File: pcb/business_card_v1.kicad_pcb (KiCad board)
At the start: 16 copper layers, 89 x 51 mm, 70 parts, among them J1 Conn_01x05_Male, J2 Conn_01x01_Male, SW1 SW_SPST, U1 MIC5504-3.3YM5, U2 STM32G030F6P6

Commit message: cleanup
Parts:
- removed J2: Conn_01x01_Male, Connector_PinSocket_2.54mm:PinSocket_1x01_P2.54mm_Vertical
- removed REF**: OSHW-Symbol_6.7x6mm_SilkScreen, Symbol:OSHW-Symbol_6.7x6mm_SilkScreen
- removed REF**: KiCad-Logo_6mm_SilkScreen, Symbol:KiCad-Logo_6mm_SilkScreen
- J1: moved to F.Cu
- RN1, RN2: footprint Resistor_SMD:R_Array_Convex_4x0603 -> Resistor_SMD:R_Array_Convex_4x1206
- SW1: value SW_SPST -> SPST_TACT-KMR2
- moved J1 10.2 mm to (132.1, 126.7)
- moved C2 1.27 mm to (126.4, 116.8)
- moved C3 1.27 mm to (128.3, 116.8)
- moved U1 1.27 mm to (127.0, 121.3)
- moved RN1 0.13 mm to (146.7, 118.1)
- moved RN2 0.13 mm to (146.7, 125.7)
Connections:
- J1 pad 2: SWDCLK-BOOT0 -> SWDIO
- J1 pad 4: SWDIO -> SWDCLK-BOOT0
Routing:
- net PINC: track 11.5 -> 13.8 mm, vias 2 -> 0
- net PINH: track 10.2 -> 8.94 mm
- net GND: track 14.6 -> 13.3 mm
- net PING: track 13.8 -> 12.8 mm, vias 2 -> 0
- net Net-(LED1-PadA): track 104.9 -> 103.8 mm
- net PINA: track 15.3 -> 16.4 mm
- net PINE: track 17.7 -> 18.7 mm
- net +5V: track 19.9 -> 20.8 mm
- net Net-(LED14-PadA): track 136.4 -> 135.6 mm
- net Net-(LED10-PadA): track 106.4 -> 105.6 mm
- net +3V3: track 1.79 -> 1.13 mm
- net Net-(LED11-PadA): track 123.5 -> 122.8 mm
- net Net-(LED10-PadC): track 136.8 -> 136.1 mm
- net Net-(LED13-PadA): track 136.1 -> 135.6 mm
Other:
- board text added: "B.E. Electrical Engineering & B.Sc. Computer Science"
- board text added: "Website: kevin.lutzer.ca Email: kevin@lutzer.ca Github: github.com/kevinlutzer LinkedIn: linkedin.com/in/kevin-lutzer"
- board text added: "v2.1"
- board text removed: "3.3V-REF"
- board text removed: "5v-SUP"
- board text removed: "B.E. Electrical Engineering & B.Sc. Computer Science Website: kevin.lutzer.ca Email: kevin@lutzer.ca Github: github.com/kevinlutzer LinkedIn: linkedin.com/in/kevin-lutzer"
- board text removed: "GND"
- board text removed: "RST"
- board text removed: "SWDCLK"
- board text removed: "SWDIO"
- board text removed: "designed with"
- board text removed: "open source"
- board text removed: "v3"

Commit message: remove the v3
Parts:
- added J2: Conn_01x01_Male, Connector_PinSocket_2.54mm:PinSocket_1x01_P2.54mm_Vertical, B.Cu at (122.5, 116.5)
- added REF**: OSHW-Symbol_6.7x6mm_SilkScreen, Symbol:OSHW-Symbol_6.7x6mm_SilkScreen, B.Cu at (141.2, 86.6)
- added REF**: KiCad-Logo_6mm_SilkScreen, Symbol:KiCad-Logo_6mm_SilkScreen, B.Cu at (114.8, 86.6)
- J1: moved to B.Cu
- RN1, RN2: footprint Resistor_SMD:R_Array_Convex_4x1206 -> Resistor_SMD:R_Array_Convex_4x0603
- SW1: value SPST_TACT-KMR2 -> SW_SPST
- moved J1 10.2 mm to (132.1, 116.5)
- moved C2 1.27 mm to (126.4, 115.6)
- moved C3 1.27 mm to (128.3, 115.6)
- moved U1 1.27 mm to (127.0, 120.0)
- moved RN1 0.13 mm to (146.6, 118.1)
- moved RN2 0.13 mm to (146.6, 125.7)
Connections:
- J1 pad 2: SWDIO -> SWDCLK-BOOT0
- J1 pad 4: SWDCLK-BOOT0 -> SWDIO
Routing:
- net PINC: track 13.8 -> 11.5 mm, vias 0 -> 2
- net PINH: track 8.94 -> 10.2 mm
- net GND: track 13.3 -> 14.6 mm
- net PING: track 12.8 -> 13.8 mm, vias 0 -> 2
- net Net-(LED1-PadA): track 103.8 -> 104.9 mm
- net PINA: track 16.4 -> 15.3 mm
- net PINE: track 18.7 -> 17.7 mm
- net +5V: track 20.8 -> 19.9 mm
- net Net-(LED14-PadA): track 135.6 -> 136.4 mm
- net Net-(LED10-PadA): track 105.6 -> 106.4 mm
- net +3V3: track 1.13 -> 1.79 mm
- net Net-(LED11-PadA): track 122.8 -> 123.5 mm
- net Net-(LED10-PadC): track 136.1 -> 136.8 mm
- net Net-(LED13-PadA): track 135.6 -> 136.1 mm
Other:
- board text added: "3.3V-REF"
- board text added: "5v-SUP"
- board text added: "B.E. Electrical Engineering & B.Sc. Computer Science Website: kevin.lutzer.ca Email: kevin@lutzer.ca Github: github.com/kevinlutzer LinkedIn: linkedin.com/in/kevin-lutzer"
- board text added: "GND"
- board text added: "RST"
- board text added: "SWDCLK"
- board text added: "SWDIO"
- board text added: "designed with"
- board text added: "open source"
- board text added: "v3"
- board text removed: "B.E. Electrical Engineering & B.Sc. Computer Science"
- board text removed: "Website: kevin.lutzer.ca Email: kevin@lutzer.ca Github: github.com/kevinlutzer LinkedIn: linkedin.com/in/kevin-lutzer"
- board text removed: "v2.1"

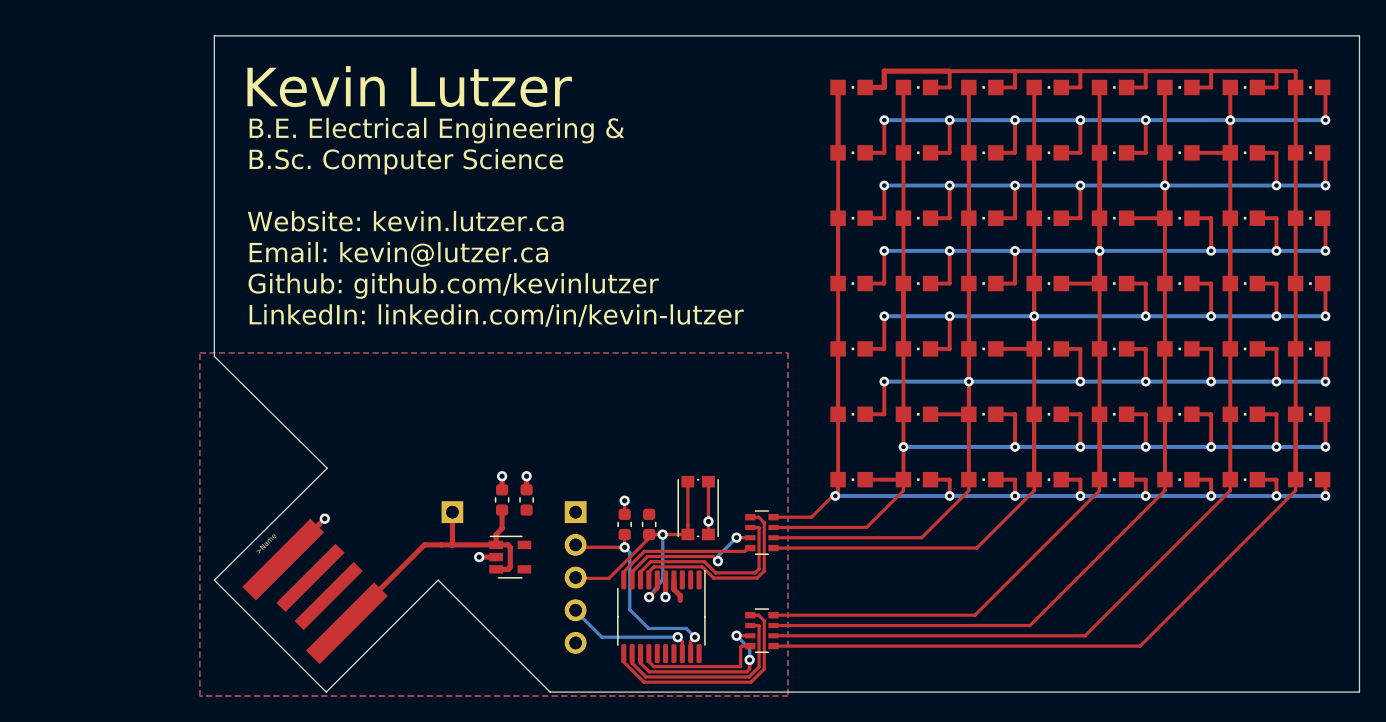
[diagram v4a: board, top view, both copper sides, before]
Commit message: realign components on 0.01 inch grid, use solely kicad parts not eagle parts
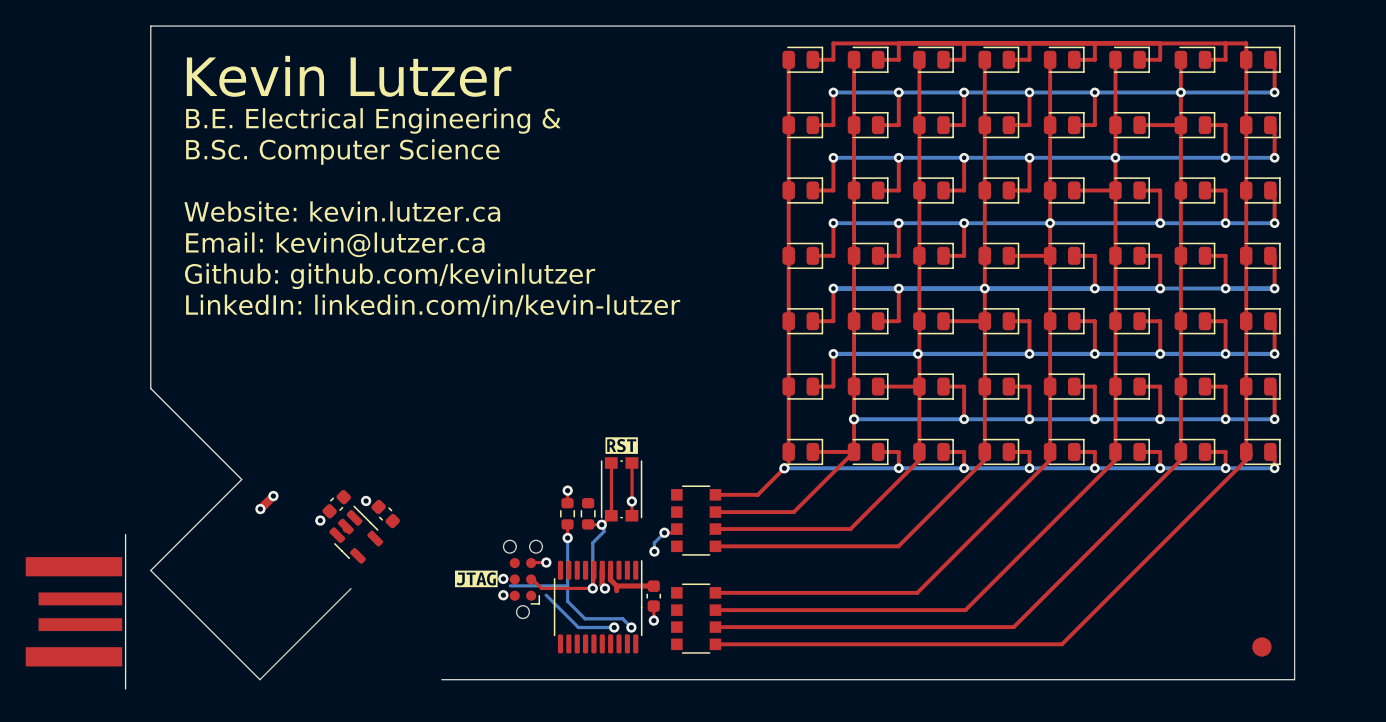
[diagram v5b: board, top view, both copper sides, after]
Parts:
- removed C3: 1u, Capacitor_SMD:C_0603_1608Metric
- removed J1: Conn_01x05_Male, Connector_PinHeader_2.54mm:PinHeader_1x05_P2.54mm_Vertical
- removed J2: Conn_01x01_Male, Connector_PinSocket_2.54mm:PinSocket_1x01_P2.54mm_Vertical
- removed JP1: USBPCB, business_card_v1:USB-A-PCB
- removed LED3: LEDCHIPLED_0805, business_card_v1:CHIPLED_0805
- removed R10: 10K, Resistor_SMD:R_0603_1608Metric
- removed the REF** at (141.2, 86.6)
- removed the REF** at (114.8, 86.6)
- added C1: 100n, Capacitor_SMD:C_0603_1608Metric, F.Cu at (138.2, 123.0)
- added C4: 1u, Capacitor_SMD:C_0603_1608Metric, F.Cu at (113.5, 115.9)
- added D7: LED, Diode_SMD:D_0805_2012Metric, F.Cu at (159.7, 81.4)
- added J3: USB_A, Kevin_Lutzer_Lbr:USB_A_PCB, F.Cu at (93.3, 124.3)
- added J4: Conn_ARM_SWD_TagConnect_TC2030, Connector:Tag-Connect_TC2030-IDC-NL_2x03_P1.27mm_Vertical, F.Cu at (128.0, 121.7)
- added R2: 10k, Resistor_SMD:R_0603_1608Metric, F.Cu at (131.5, 116.6)
- added REF**: Fiducial_1.5mm_Mask3mm, Fiducial:Fiducial_1.5mm_Mask3mm, F.Cu at (185.4, 127.0)
- added kibuzzard-64BD9765: G***, kibuzzard-64BD9765, F.Cu at (135.7, 111.3)
- added kibuzzard-64BD977B: G***, kibuzzard-64BD977B, F.Cu at (124.4, 121.7)
- D1: renamed from LED9; value LEDCHIPLED_0805 -> LED; footprint business_card_v1:CHIPLED_0805 -> Diode_SMD:D_0805_2012Metric
- D10: renamed from LED27; value LEDCHIPLED_0805 -> LED; footprint business_card_v1:CHIPLED_0805 -> Diode_SMD:D_0805_2012Metric
- D11: renamed from LED4; value LEDCHIPLED_0805 -> LED; footprint business_card_v1:CHIPLED_0805 -> Diode_SMD:D_0805_2012Metric
- D12: renamed from LED12; value LEDCHIPLED_0805 -> LED; footprint business_card_v1:CHIPLED_0805 -> Diode_SMD:D_0805_2012Metric
- D13: renamed from LED20; value LEDCHIPLED_0805 -> LED; footprint business_card_v1:CHIPLED_0805 -> Diode_SMD:D_0805_2012Metric
- D14: renamed from LED28; value LEDCHIPLED_0805 -> LED; footprint business_card_v1:CHIPLED_0805 -> Diode_SMD:D_0805_2012Metric
- D15: renamed from LED5; value LEDCHIPLED_0805 -> LED; footprint business_card_v1:CHIPLED_0805 -> Diode_SMD:D_0805_2012Metric
- D16: renamed from LED13; value LEDCHIPLED_0805 -> LED; footprint business_card_v1:CHIPLED_0805 -> Diode_SMD:D_0805_2012Metric
- D17: renamed from LED21; value LEDCHIPLED_0805 -> LED; footprint business_card_v1:CHIPLED_0805 -> Diode_SMD:D_0805_2012Metric
- D18: renamed from LED29; value LEDCHIPLED_0805 -> LED; footprint business_card_v1:CHIPLED_0805 -> Diode_SMD:D_0805_2012Metric
- D19: renamed from LED6; value LEDCHIPLED_0805 -> LED; footprint business_card_v1:CHIPLED_0805 -> Diode_SMD:D_0805_2012Metric
- D2: renamed from LED17; value LEDCHIPLED_0805 -> LED; footprint business_card_v1:CHIPLED_0805 -> Diode_SMD:D_0805_2012Metric
- D20: renamed from LED14; value LEDCHIPLED_0805 -> LED; footprint business_card_v1:CHIPLED_0805 -> Diode_SMD:D_0805_2012Metric
- D21: renamed from LED22; value LEDCHIPLED_0805 -> LED; footprint business_card_v1:CHIPLED_0805 -> Diode_SMD:D_0805_2012Metric
- D22: renamed from LED30; value LEDCHIPLED_0805 -> LED; footprint business_card_v1:CHIPLED_0805 -> Diode_SMD:D_0805_2012Metric
- D23: renamed from LED7; value LEDCHIPLED_0805 -> LED; footprint business_card_v1:CHIPLED_0805 -> Diode_SMD:D_0805_2012Metric
- D24: renamed from LED15; value LEDCHIPLED_0805 -> LED; footprint business_card_v1:CHIPLED_0805 -> Diode_SMD:D_0805_2012Metric
- D25: renamed from LED23; value LEDCHIPLED_0805 -> LED; footprint business_card_v1:CHIPLED_0805 -> Diode_SMD:D_0805_2012Metric
- D26: renamed from LED8; value LEDCHIPLED_0805 -> LED; footprint business_card_v1:CHIPLED_0805 -> Diode_SMD:D_0805_2012Metric
- D27: renamed from LED16; value LEDCHIPLED_0805 -> LED; footprint business_card_v1:CHIPLED_0805 -> Diode_SMD:D_0805_2012Metric
- D28: renamed from LED24; value LEDCHIPLED_0805 -> LED; footprint business_card_v1:CHIPLED_0805 -> Diode_SMD:D_0805_2012Metric
- D29: renamed from LED33; value LEDCHIPLED_0805 -> LED; footprint business_card_v1:CHIPLED_0805 -> Diode_SMD:D_0805_2012Metric
- D3: renamed from LED25; value LEDCHIPLED_0805 -> LED; footprint business_card_v1:CHIPLED_0805 -> Diode_SMD:D_0805_2012Metric
- D30: renamed from LED41; value LEDCHIPLED_0805 -> LED; footprint business_card_v1:CHIPLED_0805 -> Diode_SMD:D_0805_2012Metric
- D31: renamed from LED49; value LEDCHIPLED_0805 -> LED; footprint business_card_v1:CHIPLED_0805 -> Diode_SMD:D_0805_2012Metric
- D32: renamed from LED34; value LEDCHIPLED_0805 -> LED; footprint business_card_v1:CHIPLED_0805 -> Diode_SMD:D_0805_2012Metric
- D33: renamed from LED42; value LEDCHIPLED_0805 -> LED; footprint business_card_v1:CHIPLED_0805 -> Diode_SMD:D_0805_2012Metric
- D34: renamed from LED50; value LEDCHIPLED_0805 -> LED; footprint business_card_v1:CHIPLED_0805 -> Diode_SMD:D_0805_2012Metric
- D35: renamed from LED35; value LEDCHIPLED_0805 -> LED; footprint business_card_v1:CHIPLED_0805 -> Diode_SMD:D_0805_2012Metric
- D36: renamed from LED43; value LEDCHIPLED_0805 -> LED; footprint business_card_v1:CHIPLED_0805 -> Diode_SMD:D_0805_2012Metric
- D37: renamed from LED51; value LEDCHIPLED_0805 -> LED; footprint business_card_v1:CHIPLED_0805 -> Diode_SMD:D_0805_2012Metric
- D38: renamed from LED36; value LEDCHIPLED_0805 -> LED; footprint business_card_v1:CHIPLED_0805 -> Diode_SMD:D_0805_2012Metric
- D39: renamed from LED44; value LEDCHIPLED_0805 -> LED; footprint business_card_v1:CHIPLED_0805 -> Diode_SMD:D_0805_2012Metric
- D4: renamed from LED10; value LEDCHIPLED_0805 -> LED; footprint business_card_v1:CHIPLED_0805 -> Diode_SMD:D_0805_2012Metric
- D40: renamed from LED52; value LEDCHIPLED_0805 -> LED; footprint business_card_v1:CHIPLED_0805 -> Diode_SMD:D_0805_2012Metric
- D41: renamed from LED37; value LEDCHIPLED_0805 -> LED; footprint business_card_v1:CHIPLED_0805 -> Diode_SMD:D_0805_2012Metric
- D42: renamed from LED45; value LEDCHIPLED_0805 -> LED; footprint business_card_v1:CHIPLED_0805 -> Diode_SMD:D_0805_2012Metric
- D43: renamed from LED53; value LEDCHIPLED_0805 -> LED; footprint business_card_v1:CHIPLED_0805 -> Diode_SMD:D_0805_2012Metric
- D44: renamed from LED38; value LEDCHIPLED_0805 -> LED; footprint business_card_v1:CHIPLED_0805 -> Diode_SMD:D_0805_2012Metric
- D45: renamed from LED46; value LEDCHIPLED_0805 -> LED; footprint business_card_v1:CHIPLED_0805 -> Diode_SMD:D_0805_2012Metric
- D46: renamed from LED54; value LEDCHIPLED_0805 -> LED; footprint business_card_v1:CHIPLED_0805 -> Diode_SMD:D_0805_2012Metric
- D47: renamed from LED31; value LEDCHIPLED_0805 -> LED; footprint business_card_v1:CHIPLED_0805 -> Diode_SMD:D_0805_2012Metric
- D48: renamed from LED39; value LEDCHIPLED_0805 -> LED; footprint business_card_v1:CHIPLED_0805 -> Diode_SMD:D_0805_2012Metric
- D49: renamed from LED47; value LEDCHIPLED_0805 -> LED; footprint business_card_v1:CHIPLED_0805 -> Diode_SMD:D_0805_2012Metric
- D5: renamed from LED18; value LEDCHIPLED_0805 -> LED; footprint business_card_v1:CHIPLED_0805 -> Diode_SMD:D_0805_2012Metric
- D50: renamed from LED55; value LEDCHIPLED_0805 -> LED; footprint business_card_v1:CHIPLED_0805 -> Diode_SMD:D_0805_2012Metric
- D51: renamed from LED32; value LEDCHIPLED_0805 -> LED; footprint business_card_v1:CHIPLED_0805 -> Diode_SMD:D_0805_2012Metric
- D52: renamed from LED40; value LEDCHIPLED_0805 -> LED; footprint business_card_v1:CHIPLED_0805 -> Diode_SMD:D_0805_2012Metric
- D53: renamed from LED48; value LEDCHIPLED_0805 -> LED; footprint business_card_v1:CHIPLED_0805 -> Diode_SMD:D_0805_2012Metric
- D54: renamed from LED56; value LEDCHIPLED_0805 -> LED; footprint business_card_v1:CHIPLED_0805 -> Diode_SMD:D_0805_2012Metric
- D6: renamed from LED26; value LEDCHIPLED_0805 -> LED; footprint business_card_v1:CHIPLED_0805 -> Diode_SMD:D_0805_2012Metric
- D8: renamed from LED11; value LEDCHIPLED_0805 -> LED; footprint business_card_v1:CHIPLED_0805 -> Diode_SMD:D_0805_2012Metric
- D9: renamed from LED19; value LEDCHIPLED_0805 -> LED; footprint business_card_v1:CHIPLED_0805 -> Diode_SMD:D_0805_2012Metric
- LED1, LED2: footprint business_card_v1:CHIPLED_0805 -> Diode_SMD:D_0805_2012Metric
- R1: value 10K -> 10k
- RN1, RN2: footprint Resistor_SMD:R_Array_Convex_4x0603 -> Resistor_SMD:R_Array_Convex_4x1206
- moved U1 12.1 mm to (115.0, 118.4), turned to -45 degrees
- moved C2 9.11 mm to (117.3, 116.7), turned to 135 degrees
- moved SW1 6.13 mm to (135.7, 114.7)
- moved RN1 5.20 mm to (141.4, 117.2)
- moved RN2 5.20 mm to (141.4, 124.8)
- moved U2 4.98 mm to (133.8, 123.9)
- moved D10 4.50 mm to (159.7, 96.6), turned to 180 degrees
- moved D18 4.50 mm to (169.9, 96.6), turned to 180 degrees
- moved D29 4.50 mm to (149.6, 101.7), turned to 180 degrees
- moved D3 4.50 mm to (149.6, 96.6), turned to 180 degrees
- moved D30 4.50 mm to (149.6, 106.8), turned to 180 degrees
- moved D31 4.50 mm to (149.6, 111.8), turned to 180 degrees
- moved D35 4.50 mm to (159.7, 101.7), turned to 180 degrees
- moved D36 4.50 mm to (159.7, 106.8), turned to 180 degrees
- moved D37 4.50 mm to (159.7, 111.8), turned to 180 degrees
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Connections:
- C2 pad 1: +5V -> +3V3
- R1 pad 1: SWDCLK-BOOT0 -> +3V3
- R1 pad 2: GND -> ~{RST}
- RN1 pad 5: Net-(LED12-PadA) -> /PIND_R
- RN1 pad 6: Net-(LED11-PadA) -> /PINC_R
- RN1 pad 7: Net-(LED10-PadA) -> /PINB_R
- RN1 pad 8: Net-(LED1-PadA) -> /PINA_R
- RN2 pad 5: Net-(LED1-PadC) -> /PING_H
- RN2 pad 6: Net-(LED10-PadC) -> /PING_R
- RN2 pad 7: Net-(LED14-PadA) -> /PINF_R
- RN2 pad 8: Net-(LED13-PadA) -> /PINE_R
- SW1 pad 1: RST -> ~{RST}
- U1 pad 4: (no net) -> unconnected-(U1-NC-Pad4)
- U2 pad 1: (no net) -> unconnected-(U2-PB7/PB8-Pad1)
- U2 pad 15: (no net) -> unconnected-(U2-PB0/PB1/PB2/PA8-Pad15)
- U2 pad 16: (no net) -> unconnected-(U2-PA11[PA9]-Pad16)
- U2 pad 17: (no net) -> unconnected-(U2-PA12[PA10]-Pad17)
- U2 pad 19: SWDCLK-BOOT0 -> SWDCLK
- U2 pad 2: (no net) -> unconnected-(U2-PB9/PC14-OSC32_IN-Pad2)
- U2 pad 20: (no net) -> unconnected-(U2-PB3/PB4/PB5/PB6-Pad20)
- U2 pad 3: (no net) -> unconnected-(U2-PC15-OSC32_OUT-Pad3)
- U2 pad 6: RST -> ~{RST}
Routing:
- net /PING_H: track 0.00 -> 151.8 mm
- net /PIND_R: track 0.00 -> 144.3 mm, vias 0 -> 7
- net /PINC_R: track 0.00 -> 138.4 mm, vias 0 -> 7
- net Net-(LED10-PadC): track 136.8 -> 0.00 mm, vias 7 -> 0
- net Net-(LED14-PadA): track 136.4 -> 0.00 mm, vias 7 -> 0
- net Net-(LED13-PadA): track 136.1 -> 0.00 mm, vias 7 -> 0
- net Net-(LED1-PadC): track 134.6 -> 0.00 mm
- net /PING_R: track 0.00 -> 132.8 mm, vias 0 -> 7
- net Net-(LED12-PadA): track 128.9 -> 0.00 mm, vias 7 -> 0
- net /PINF_R: track 0.00 -> 127.0 mm, vias 0 -> 7
- net Net-(LED11-PadA): track 123.5 -> 0.00 mm, vias 7 -> 0
- net /PINE_R: track 0.00 -> 121.4 mm, vias 0 -> 7
- net Net-(LED10-PadA): track 106.4 -> 0.00 mm, vias 7 -> 0
- net Net-(LED1-PadA): track 104.9 -> 0.00 mm, vias 8 -> 0
- net /PINB_R: track 0.00 -> 101.9 mm, vias 0 -> 7
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- removed copper zone on F.Cu, net +3V3
- removed copper zone on B.Cu, net GND
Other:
- board size 89 x 51 mm -> 88.9 x 50.8 mm
- net class Default removed
- rule solder_mask_min_width: 0.25 -> 0.1
- board text added: "Placed 0.01/0.1 inch Routed 0.001 inch"
- board text added: "v4"
- board text removed: "3.3V-REF"
- board text removed: "5v-SUP"
- board text removed: "GND"
- board text removed: "RST"
- board text removed: "SWDCLK"
- board text removed: "SWDIO"
- board text removed: "designed with"
- board text removed: "open source"
- board text removed: "v3"
